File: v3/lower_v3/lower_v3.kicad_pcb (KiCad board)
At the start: 2 copper layers, 40.6 x 64.8 mm, 7 parts, among them J1 Conn_01x05_Male, J2 Conn_01x05_Male, J3 Conn_01x21, J4 Conn_01x02_Male, U1 ESP32-DEVKIT-V1

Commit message: Rev.A Toast Design, fixing connection between 2 boards, adding 3 I/O for the DOME, creating blank proto area for testing
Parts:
- J2: value Conn_01x05_Male -> Conn_01x06_Male; footprint Connector_PinHeader_2.54mm:PinHeader_1x05_P2.54mm_Vertical -> Connector_PinHeader_2.54mm:PinHeader_1x06_P2.54mm_Vertical
- moved J2 1.28 mm to (137.2, 77.5)
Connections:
- J2 pad 1: Net-(J2-Pad1) -> Net-(J3-Pad11)
- J2 pad 2: Net-(J2-Pad2) -> Net-(U1-Pad28)
- J2 pad 3: Net-(J2-Pad3) -> Net-(U1-Pad27)
- J2 pad 4: Net-(J2-Pad4) -> Net-(U1-Pad5)
- J2 pad 5: GND -> Net-(U1-Pad4)
- U1 pad 27: Net-(J2-Pad2) -> Net-(U1-Pad27)
- U1 pad 28: Net-(J2-Pad1) -> Net-(U1-Pad28)
- U1 pad 4: Net-(J2-Pad4) -> Net-(U1-Pad4)
- U1 pad 5: Net-(J2-Pad3) -> Net-(U1-Pad5)
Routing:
- net Net-(J2-Pad3): track 29.1 -> 0.00 mm
- net Net-(U1-Pad5): track 0.00 -> 28.8 mm
- net Net-(U1-Pad27): track 0.00 -> 26.2 mm
- net Net-(J2-Pad2): track 25.5 -> 0.00 mm
- net Net-(J2-Pad4): track 25.5 -> 0.00 mm
- net Net-(U1-Pad4): track 0.00 -> 25.0 mm
- net Net-(U1-Pad28): track 0.00 -> 22.6 mm
- net Net-(J2-Pad1): track 21.9 -> 0.00 mm
- net Net-(J3-Pad11): track 75.4 -> 84.0 mm
- net GND: track 119.1 -> 122.5 mm

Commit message: With OshPark order
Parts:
- removed N1: Housing, Filter:Filter_1109-5_1.1x0.9mm
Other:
- board text added: "ClearGauntlet Rev.A"
- board text removed: "ClearGauntlet"
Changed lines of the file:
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@@
       (layerselection 0x00010fc_ffffffff)
       (disableapertmacros false)
-      (usegerberextensions false)
+      (usegerberextensions true)
       (usegerberattributes true)
       (usegerberadvancedattributes true)
@@
       (svguseinch false)
       (svgprecision 6)
-      (excludeedgelayer true)
+      (excludeedgelayer false)
       (plotframeref false)
       (viasonmask false)
@@
       (outputformat 1)
       (mirror false)
-      (drillshape 1)
+      (drillshape 0)
       (scaleselection 1)
-      (outputdirectory "")
+      (outputdirectory "lower-gerber/")
     )
   )
@@
     )
   )
-  (footprint "Filter:Filter_1109-5_1.1x0.9mm" (layer "F.Cu")
-    (at 118.11 77.47)
-    (descr "5-pin SAW filter package - 1.1x0.9 mm Body; (see https://www.murata.com/~/media/webrenewal/support/library/catalog/products/filter/rf/p73e.ashx?la=en-gb)")
-    (tags "Filter 5")
-    (property "Sheetfile" "lower_v3.kicad_sch")
-    (property "Sheetname" "")
-    (attr smd)
-    (fp_text reference "N1" (at -1.27 1.6) (layer "F.SilkS")
-      (effects (font (size 1 1) (thickness 0.15)))
-    )
-    (fp_text value "Housing" (at 0 -1.4) (layer "F.Fab")
-      (effects (font (size 1 1) (thickness 0.15)))
-    )
-    (fp_text user "${REFERENCE}" (at 0 -2.7) (layer "F.Fab")
-      (effects (font (size 1 1) (thickness 0.15)))
-    )
-    (fp_line (start -0.6 -0.5) (end -0.6 0.5) (layer "F.SilkS") (width 0.12))
-    (fp_line (start 0.6 -0.5) (end -0.6 -0.5) (layer "F.SilkS") (width 0.12))
-    (fp_line (start -0.75 -0.5) (end -0.75 0.5) (layer "F.SilkS") (width 0.12))
-    (fp_line (start -0.6 0.5) (end 0.6 0.5) (layer "F.SilkS") (width 0.12))
-    (fp_line (start 0.6 0.5) (end 0.6 -0.5) (layer "F.SilkS") (width 0.12))
-    (fp_line (start -0.7 -0.6) (end 0.7 -0.6) (layer "F.CrtYd") (width 0.05))
-    (fp_line (start 0.7 0.6) (end -0.7 0.6) (layer "F.CrtYd") (width 0.05))
-    (fp_line (start 0.7 -0.6) (end 0.7 0.6) (layer "F.CrtYd") (width 0.05))
-    (fp_line (start -0.7 0.6) (end -0.7 -0.6) (layer "F.CrtYd") (width 0.05))
-    (fp_line (start -0.55 0.15) (end -0.55 0.45) (layer "F.Fab") (width 0.1))
-    (fp_line (start 0.55 0.45) (end -0.55 0.45) (layer "F.Fab") (width 0.1))
-    (fp_line (start -0.4 0) (end -0.55 0.15) (layer "F.Fab") (width 0.1))
-    (fp_line (start -0.55 -0.15) (end -0.4 0) (layer "F.Fab") (width 0.1))
-    (fp_line (start -0.55 -0.45) (end -0.55 -0.15) (layer "F.Fab") (width 0.1))
-    (fp_line (start 0.55 -0.45) (end 0.55 0.45) (layer "F.Fab") (width 0.1))
-    (fp_line (start -0.55 -0.45) (end 0.55 -0.45) (layer "F.Fab") (width 0.1))
-    (pad "1" smd rect (at -0.385 0 90) (size 0.25 0.18) (layers "F.Cu" "F.Paste" "F.Mask"))
-    (pad "2" smd rect (at 0 0.25 90) (size 0.25 0.18) (layers "F.Cu" "F.Paste" "F.Mask"))
-    (pad "3" smd rect (at 0.385 0.25 90) (size 0.25 0.18) (layers "F.Cu" "F.Paste" "F.Mask"))
-    (pad "4" smd rect (at 0.385 -0.25 90) (size 0.25 0.18) (layers "F.Cu" "F.Paste" "F.Mask"))
-    (pad "5" smd rect (at 0 -0.25 90) (size 0.25 0.18) (layers "F.Cu" "F.Paste" "F.Mask"))
-    (model "${KICAD6_3DMODEL_DIR}/Filter.3dshapes/Filter_1109-5_1.1x0.9mm.wrl"
-      (offset (xyz 151.5 588 0))
-      (scale (xyz 1 1 1))
-      (rotate (xyz 0 0 0))
-    )
-    (model "C:/Users/Long Nguyen/Documents/RIT/RIT_Fall_22/MSD/ClearGauntlet-PCB/v3/upper_v3/toast_upper.STEP"
-      (offset (xyz -120 63.5 -10.5))
-      (scale (xyz 1 1 1))
-      (rotate (xyz 0 0 0))
-    )
-  )
   (footprint "Connector_PinHeader_2.54mm:PinHeader_1x21_P2.54mm_Horizontal" (layer "F.Cu")
     (at 151.13 78.74)
@@
   )
   (gr_rect (start 154.94 138.43) (end 114.3 73.66) (layer "Edge.Cuts") (width 0.1) (fill none))
-  (gr_text "ClearGauntlet\n" (at 130.81 116.84) (layer "F.SilkS")
+  (gr_text "ClearGauntlet\nRev.A\n" (at 130.81 116.84) (layer "F.SilkS")
     (effects (font (size 1.5 1.5) (thickness 0.3)))
   )

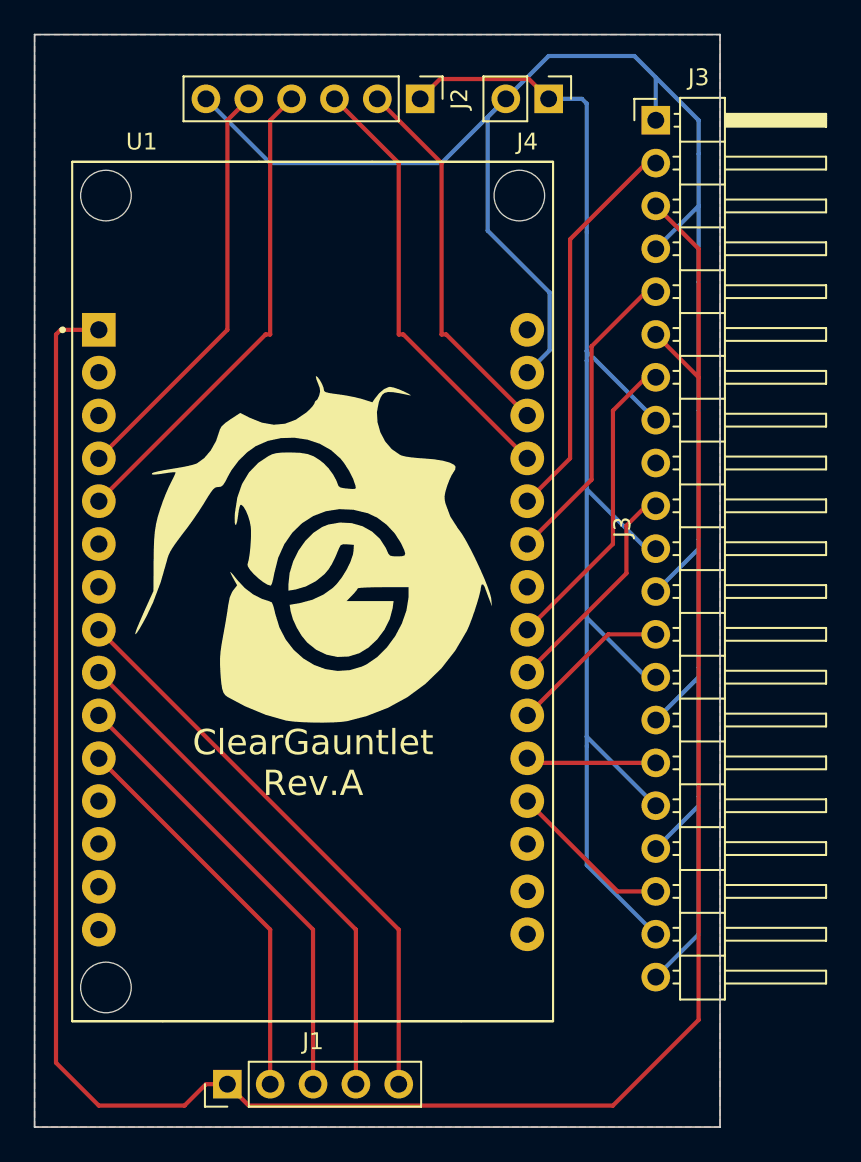
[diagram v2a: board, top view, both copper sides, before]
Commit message: Add pin detail, fixing layout annotation on board
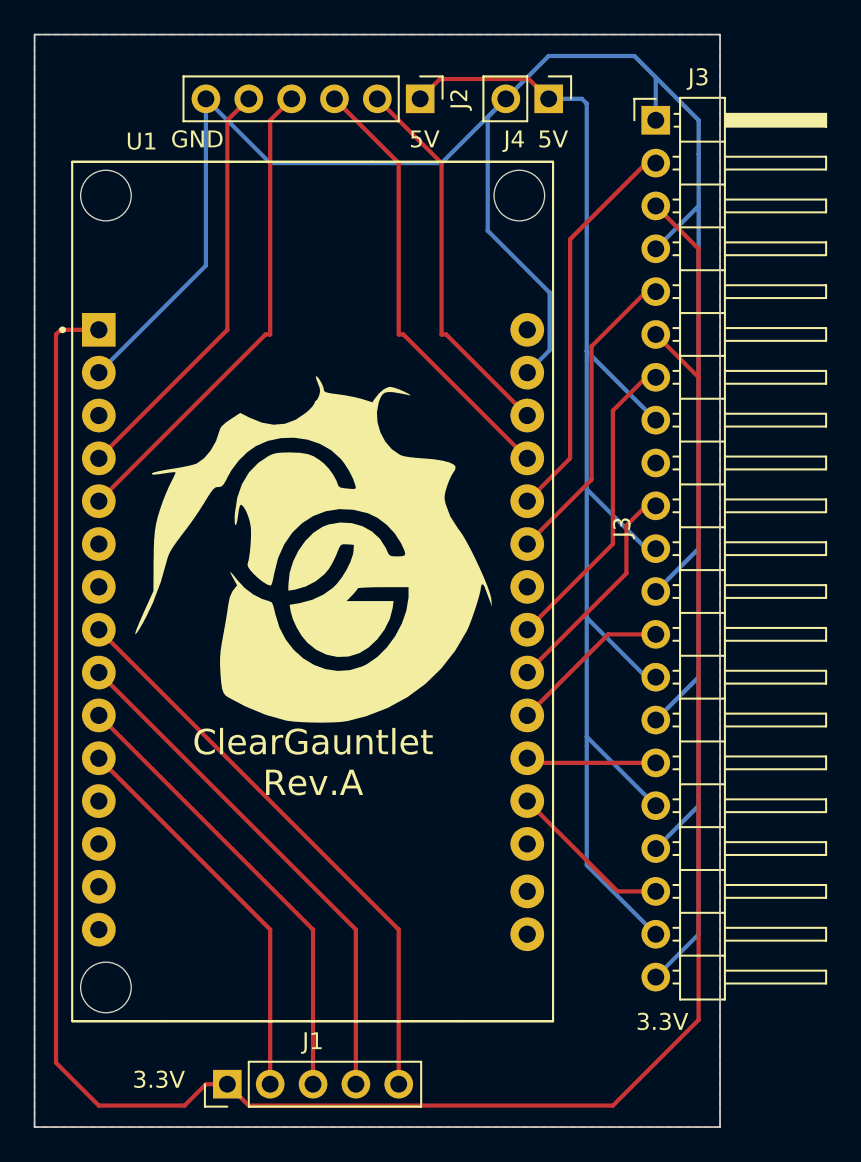
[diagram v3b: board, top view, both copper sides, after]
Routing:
- net GND: track 122.5 -> 141.4 mm
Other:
- board text added: "3.3V"
- board text added: "5V"
- board text added: "GND"
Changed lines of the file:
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@@
     (property "Sheetname" "")
     (attr through_hole)
-    (fp_text reference "J4" (at 2.54 1.27 180) (layer "F.SilkS")
+    (fp_text reference "J4" (at 2.413 2.032 180) (layer "F.SilkS")
       (effects (font (size 1 1) (thickness 0.15)))
     )
@@
   )
   (gr_rect (start 154.94 138.43) (end 114.3 73.66) (layer "Edge.Cuts") (width 0.1) (fill none))
+  (gr_text "5V" (at 137.414 79.883) (layer "B.SilkS")
+    (effects (font (size 1 1) (thickness 0.15)) (justify mirror))
+  )
+  (gr_text "GND" (at 148.463 106.68) (layer "B.SilkS")
+    (effects (font (size 1 1) (thickness 0.15)) (justify mirror))
+  )
+  (gr_text "GND" (at 153.289 76.2) (layer "B.SilkS")
+    (effects (font (size 1 1) (thickness 0.15)) (justify mirror))
+  )
+  (gr_text "GND" (at 140.589 93.726) (layer "B.SilkS")
+    (effects (font (size 1 1) (thickness 0.15)) (justify mirror))
+  )
+  (gr_text "5V" (at 145.034 79.883) (layer "B.SilkS")
+    (effects (font (size 1 1) (thickness 0.15)) (justify mirror))
+  )
+  (gr_text "GND" (at 123.952 79.883) (layer "B.SilkS")
+    (effects (font (size 1 1) (thickness 0.15)) (justify mirror))
+  )
+  (gr_text "5V" (at 148.463 96.012) (layer "B.SilkS")
+    (effects (font (size 1 1) (thickness 0.15)) (justify mirror))
+  )
+  (gr_text "GND" (at 148.463 129.667) (layer "B.SilkS")
+    (effects (font (size 1 1) (thickness 0.15)) (justify mirror))
+  )
+  (gr_text "3.3V" (at 121.666 135.763) (layer "B.SilkS")
+    (effects (font (size 1 1) (thickness 0.15)) (justify mirror))
+  )
+  (gr_text "5V" (at 148.59 126.746) (layer "B.SilkS")
+    (effects (font (size 1 1) (thickness 0.15)) (justify mirror))
+  )
+  (gr_text "5V" (at 145.034 79.883) (layer "F.SilkS")
+    (effects (font (size 1 1) (thickness 0.15)))
+  )
   (gr_text "ClearGauntlet\nRev.A\n" (at 130.81 116.84) (layer "F.SilkS")
     (effects (font (size 1.5 1.5) (thickness 0.3)))
+  )
+  (gr_text "3.3V" (at 121.666 135.636) (layer "F.SilkS")
+    (effects (font (size 1 1) (thickness 0.15)))
+  )
+  (gr_text "5V" (at 137.414 79.883) (layer "F.SilkS")
+    (effects (font (size 1 1) (thickness 0.15)))
+  )
+  (gr_text "GND" (at 123.952 79.883) (layer "F.SilkS")
+    (effects (font (size 1 1) (thickness 0.15)))
+  )
+  (gr_text "3.3V" (at 151.511 132.207) (layer "F.SilkS")
+    (effects (font (size 1 1) (thickness 0.15)))
   )
   (segment (start 149.86 74.93) (end 151.13 76.2) (width 0.25) (layer "B.Cu") (net 4))
@@
   (segment (start 153.67 127) (end 153.67 118.815) (width 0.25) (layer "B.Cu") (net 4))
   (segment (start 153.67 78.74) (end 153.67 80.715) (width 0.25) (layer "B.Cu") (net 4))
+  (segment (start 124.46 77.47) (end 124.46 87.355) (width 0.25) (layer "B.Cu") (net 4))
   (segment (start 141.164999 85.284999) (end 141.164999 78.545001) (width 0.25) (layer "B.Cu") (net 4))
   (segment (start 128.27 81.28) (end 124.46 77.47) (width 0.25) (layer "B.Cu") (net 4))
@@
   (segment (start 153.67 103.575) (end 153.67 111.195) (width 0.25) (layer "B.Cu") (net 4))
   (segment (start 153.67 80.715) (end 153.67 83.82) (width 0.25) (layer "B.Cu") (net 4))
+  (segment (start 124.46 87.355) (end 118.11 93.705) (width 0.25) (layer "B.Cu") (net 4))
   (segment (start 151.13 86.36) (end 153.67 83.82) (width 0.25) (layer "B.Cu") (net 4))
   (segment (start 138.43 81.28) (end 128.27 81.28) (width 0.25) (layer "B.Cu") (net 4))

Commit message: Add more pins
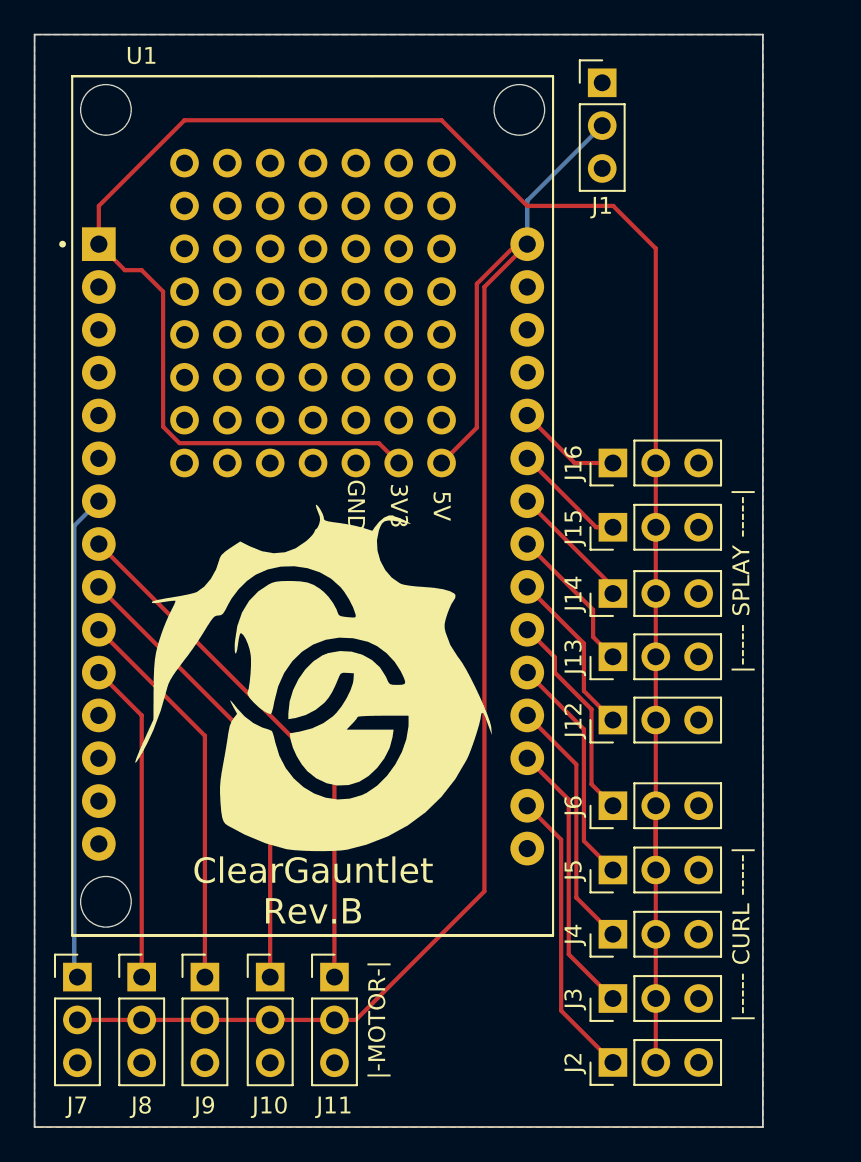
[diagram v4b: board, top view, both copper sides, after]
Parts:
- added 83: , , F.Cu at (128.3, 83.8)
- added 83: , , F.Cu at (128.3, 86.4)
- added 83: , , F.Cu at (128.3, 94.0)
- added 83: , , F.Cu at (128.3, 96.5)
- added 83: , , F.Cu at (133.3, 99.1)
- added 83: , , F.Cu at (128.3, 91.4)
- added 83: , , F.Cu at (123.2, 96.5)
- added 83: , , F.Cu at (123.2, 99.1)
- added 83: , , F.Cu at (133.3, 81.3)
- added 83: , , F.Cu at (128.3, 81.3)
- added 83: , , F.Cu at (123.2, 81.3)
- added 83: , , F.Cu at (133.3, 88.9)
- added 83: , , F.Cu at (123.2, 88.9)
- added 83: , , F.Cu at (133.3, 86.4)
- added 83: , , F.Cu at (133.3, 91.4)
- added 83: , , F.Cu at (128.3, 99.1)
- added 83: , , F.Cu at (123.2, 91.4)
- added 83: , , F.Cu at (128.3, 88.9)
- added 83: , , F.Cu at (123.2, 83.8)
- added 83: , , F.Cu at (123.2, 86.4)
- added 83: , , F.Cu at (123.2, 94.0)
- added 83: , , F.Cu at (133.3, 83.8)
- added 83: , , F.Cu at (133.3, 96.5)
- added 83: , , F.Cu at (133.3, 94.0)
- added 84: , , F.Cu at (135.9, 81.3)
- added 84: , , F.Cu at (130.8, 91.4)
- added 84: , , F.Cu at (130.8, 96.5)
- added 84: , , F.Cu at (135.9, 83.8)
- added 84: , , F.Cu at (125.7, 99.1)
- added 84: , , F.Cu at (135.9, 96.5)
- added 84: , , F.Cu at (130.8, 99.1)
- added 84: , , F.Cu at (135.9, 99.1)
- added 84: , , F.Cu at (125.7, 96.5)
- added 84: , , F.Cu at (135.9, 86.4)
- added 84: , , F.Cu at (138.4, 94.0)
- added 84: , , F.Cu at (125.7, 91.4)
- added 84: , , F.Cu at (130.8, 81.3)
- added 84: , , F.Cu at (138.4, 88.9)
- added 84: , , F.Cu at (125.7, 94.0)
- added 84: , , F.Cu at (138.4, 81.3)
- added 84: , , F.Cu at (125.7, 86.4)
- added 84: , , F.Cu at (130.8, 83.8)
- added 84: , , F.Cu at (135.9, 88.9)
- added 84: , , F.Cu at (125.7, 83.8)
- added 84: , , F.Cu at (138.4, 99.1)
- added 84: , , F.Cu at (138.4, 83.8)
- added 84: , , F.Cu at (130.8, 88.9)
- added 84: , , F.Cu at (138.4, 86.4)
- added 84: , , F.Cu at (125.7, 81.3)
- added 84: , , F.Cu at (138.4, 91.4)
- added 84: , , F.Cu at (135.9, 91.4)
- added 84: , , F.Cu at (130.8, 94.0)
- added 84: , , F.Cu at (130.8, 86.4)
- added 84: , , F.Cu at (135.9, 94.0)
- added 84: , , F.Cu at (138.4, 96.5)
- added 84: , , F.Cu at (125.7, 88.9)
- added J10: PIN_RING_MOTOR, Connector_PinHeader_2.54mm:PinHeader_1x03_P2.54mm_Vertical, F.Cu at (128.3, 129.5)
- added J11: PIN_PINKY_MOTOR, Connector_PinHeader_2.54mm:PinHeader_1x03_P2.54mm_Vertical, F.Cu at (132.1, 129.5)
- added J12: PIN_PINKY_SPLAY, Connector_PinHeader_2.54mm:PinHeader_1x03_P2.54mm_Vertical, F.Cu at (148.6, 114.3)
- added J13: PIN_RING_SPLAY, Connector_PinHeader_2.54mm:PinHeader_1x03_P2.54mm_Vertical, F.Cu at (148.6, 110.5)
- added J14: PIN_MIDDLE_SPLAY, Connector_PinHeader_2.54mm:PinHeader_1x03_P2.54mm_Vertical, F.Cu at (148.6, 106.8)
- added J15: PIN_INDEX_SPLAY, Connector_PinHeader_2.54mm:PinHeader_1x03_P2.54mm_Vertical, F.Cu at (148.6, 102.9)
- added J16: PIN_THUMB_SPLAY, Connector_PinHeader_2.54mm:PinHeader_1x03_P2.54mm_Vertical, F.Cu at (148.6, 99.1)
- added J5: PIN_INDEX, Connector_PinHeader_2.54mm:PinHeader_1x03_P2.54mm_Vertical, F.Cu at (148.6, 123.2)
- added J6: PIN_THUMB, Connector_PinHeader_2.54mm:PinHeader_1x03_P2.54mm_Vertical, F.Cu at (148.6, 119.4)
- added J7: PIN_THUMB_MOTOR, Connector_PinHeader_2.54mm:PinHeader_1x03_P2.54mm_Vertical, F.Cu at (116.8, 129.5)
- added J8: PIN_INDEX_MOTOR, Connector_PinHeader_2.54mm:PinHeader_1x03_P2.54mm_Vertical, F.Cu at (120.7, 129.5)
- added J9: PIN_MIDDLE_MOTOR, Connector_PinHeader_2.54mm:PinHeader_1x03_P2.54mm_Vertical, F.Cu at (124.4, 129.5)
- J1: value Conn_01x05_Male -> To Power Bank; footprint Connector_PinHeader_2.54mm:PinHeader_1x05_P2.54mm_Vertical -> Connector_PinHeader_2.54mm:PinHeader_1x03_P2.54mm_Vertical
- J2: value Conn_01x06_Male -> PIN_PINKY; footprint Connector_PinHeader_2.54mm:PinHeader_1x06_P2.54mm_Vertical -> Connector_PinHeader_2.54mm:PinHeader_1x03_P2.54mm_Vertical
- J3: value Conn_01x21 -> PIN_RING; footprint Connector_PinHeader_2.54mm:PinHeader_1x21_P2.54mm_Horizontal -> Connector_PinHeader_2.54mm:PinHeader_1x03_P2.54mm_Vertical
- J4: value Conn_01x02_Male -> PIN_MIDDLE; footprint Connector_PinHeader_2.54mm:PinHeader_1x02_P2.54mm_Vertical -> Connector_PinHeader_2.54mm:PinHeader_1x03_P2.54mm_Vertical
- moved J1 63.4 mm to (148.0, 76.5), turned to 0 degrees
- moved J2 58.3 mm to (148.6, 134.6), turned to 90 degrees
- moved J3 52.1 mm to (148.6, 130.8), turned to 90 degrees
- moved J4 49.7 mm to (148.6, 127.0), turned to 90 degrees
- moved logo 7.62 mm to (130.8, 111.8)
- moved U1 5.08 mm to (130.8, 101.6)
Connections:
- J1 pad 1: Net-(J1-Pad1) -> GND
- J1 pad 2: Net-(J1-Pad2) -> 5V
- J1 pad 3: Net-(J1-Pad3) -> GND
- J2 pad 1: Net-(J3-Pad11) -> Net-(J2-Pad1)
- J2 pad 2: Net-(U1-Pad28) -> Net-(J2-Pad2)
- J2 pad 3: Net-(U1-Pad27) -> GND
- J3 pad 1: GND -> Net-(J3-Pad1)
- J3 pad 2: Net-(J3-Pad2) -> Net-(J2-Pad2)
- J3 pad 3: Net-(J1-Pad1) -> GND
- J4 pad 1: Net-(J3-Pad11) -> Net-(J4-Pad1)
- J4 pad 2: GND -> Net-(J2-Pad2)
- U1 pad 10: Net-(J1-Pad3) -> Net-(J4-Pad1)
- U1 pad 11: Net-(J1-Pad2) -> Net-(J5-Pad1)
- U1 pad 12: unconnected-(U1-Pad12) -> Net-(J6-Pad1)
- U1 pad 13: unconnected-(U1-Pad13) -> Net-(U1-Pad13)
- U1 pad 14: unconnected-(U1-Pad14) -> Net-(U1-Pad14)
- U1 pad 15: unconnected-(U1-Pad15) -> Net-(U1-Pad15)
- U1 pad 16: unconnected-(U1-Pad16) -> Net-(U1-Pad16)
- U1 pad 17: unconnected-(U1-Pad17) -> Net-(U1-Pad17)
- U1 pad 20: Net-(J3-Pad16) -> unconnected-(U1-Pad20)
- U1 pad 21: Net-(J3-Pad13) -> unconnected-(U1-Pad21)
- U1 pad 22: Net-(J3-Pad10) -> unconnected-(U1-Pad22)
- U1 pad 25: Net-(J3-Pad5) -> unconnected-(U1-Pad25)
- U1 pad 27: Net-(U1-Pad27) -> Net-(J7-Pad1)
- U1 pad 5: Net-(U1-Pad5) -> Net-(J2-Pad1)
- U1 pad 8: Net-(J1-Pad5) -> Net-(J3-Pad1)
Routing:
- net GND: track 141.4 -> 0.00 mm
- net Net-(J1-Pad1): track 141.0 -> 0.00 mm
- net Net-(J2-Pad2): track 0.00 -> 93.9 mm
- net Net-(J3-Pad11): track 84.0 -> 0.00 mm
- net Net-(J1-Pad2): track 23.5 -> 66.7 mm
- net Net-(J1-Pad5): track 34.3 -> 0.00 mm
- net Net-(J11-Pad1): track 0.00 -> 31.5 mm
- net Net-(J1-Pad4): track 30.7 -> 0.00 mm
- net Net-(J7-Pad1): track 0.00 -> 28.9 mm
- net Net-(U1-Pad5): track 28.8 -> 0.00 mm
- net 3V3: track 0.00 -> 27.7 mm
- net Net-(J10-Pad1): track 0.00 -> 27.3 mm
- net Net-(J1-Pad3): track 27.1 -> 0.00 mm
- net Net-(U1-Pad27): track 26.2 -> 0.00 mm
- net Net-(U1-Pad4): track 25.0 -> 0.00 mm
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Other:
- board size 40.6 x 64.8 mm -> 43.2 x 64.8 mm
- board text added: "3V3"
- board text added: "ClearGauntlet Rev.B"
- board text added: "|----- CURL -----|"
- board text added: "|----- SPLAY -----|"
- board text added: "|-MOTOR-|"
- board text removed: "3.3V"
- board text removed: "ClearGauntlet Rev.A"
